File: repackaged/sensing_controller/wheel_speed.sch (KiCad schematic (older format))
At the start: 41 parts, among them J1 CONN_02X03, J2 MM_F_RA_08, U1 MCP2561-E_SN, U101 TPS560430YF, U2 ATMEGA16M1, Y1 Crystal_SMD

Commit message: Change VCC to +5V.
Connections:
- net labels added: +5V
- net labels removed: VCC
- wire segments 109 -> 108
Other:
- note removed: "5V"
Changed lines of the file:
@@
 $Descr A4 11693 8268
 encoding utf-8
-Sheet 1 25
+Sheet 20 25
 Title "Wheel Speed Sensing"
 Date "2019-11-17"
@@
 U 1 1 6102CC1A
 P 6000 6200
-F 0 "R104" V 5800 6200 50  0000 C CNN
-F 1 "R_0_2512" V 5900 6250 50  0000 C CNN
+F 0 "R104" V 5748 6126 50  0000 C CNN
+F 1 "R_0_2512" V 5850 6112 50  0000 C CNN
 F 2 "footprints:R_2512_OEM" H 5930 6200 50  0001 C CNN
 F 3 "http://www.te.com/commerce/DocumentDelivery/DDEController?Action=srchrtrv&DocNm=9-1773463-7&DocType=DS&DocLang=English" H 6080 6200 50  0001 C CNN
@@
 U 1 1 6102CC29
 P 1550 6650
-F 0 "D102" V 1588 6533 50  0000 R CNN
-F 1 "LED_0805" V 1497 6533 50  0000 R CNN
+F 0 "D102" V 1476 6408 50  0000 R CNN
+F 1 "LED_0805" V 1384 6486 50  0000 R CNN
 F 2 "footprints:LED_0805_OEM" H 1450 6650 50  0001 C CNN
 F 3 "http://www.osram-os.com/Graphics/XPic9/00078860_0.pdf" H 1550 6750 50  0001 C CNN
@@
 Text Notes 5800 6100 0    50   ~ 0
 VCC Jumper\n
-$Comp
-L power:VCC #PWR0112
-U 1 1 6102CC26
-P 6400 6050
-F 0 "#PWR0112" H 6400 5900 50  0001 C CNN
-F 1 "VCC" H 6417 6223 50  0000 C CNN
-F 2 "" H 6400 6050 50  0001 C CNN
-F 3 "" H 6400 6050 50  0001 C CNN
-	1    6400 6050
-	1    0    0    -1
-$EndComp
-Text Notes 6500 6000 0    50   ~ 0
-5V
 Text Notes 6250 7300 1    50   ~ 0
 5V Indicator
@@
 U 1 1 6102CC43
 P 4100 4100
-F 0 "Y1" H 3810 4170 50  0000 L CNN
+F 0 "Y1" H 3644 4174 50  0000 L CNN
 F 1 "Crystal_SMD" H 3420 4100 50  0000 L CNN
 F 2 "footprints:Crystal_SMD_FA238" H 4050 4175 50  0001 C CNN
@@
 U 1 1 6102CC46
 P 3900 4350
-F 0 "C4" H 3790 4430 50  0000 L CNN
+F 0 "C4" H 3684 4356 50  0000 L CNN
 F 1 "C_30pF" H 3630 4270 50  0000 L CNN
 F 2 "footprints:C_0805_OEM" H 3938 4200 50  0001 C CNN
@@
 U 1 1 6102CC48
 P 4300 4350
-F 0 "C5" H 4320 4430 50  0000 L CNN
+F 0 "C5" H 4424 4340 50  0000 L CNN
 F 1 "C_30pF" H 4330 4250 50  0000 L CNN
 F 2 "footprints:C_0805_OEM" H 4338 4200 50  0001 C CNN
@@
 $EndComp
 $Comp
-L power:VCC #PWR08
-U 1 1 6102CC54
-P 4450 3350
-F 0 "#PWR08" H 4450 3200 50  0001 C CNN
-F 1 "VCC" H 4560 3410 50  0000 C CNN
-F 2 "" H 4450 3350 50  0001 C CNN
-F 3 "" H 4450 3350 50  0001 C CNN
-	1    4450 3350
-	1    0    0    -1
-$EndComp
-$Comp
 L power:GND #PWR011
 U 1 1 5D5F86E8
@@
 $EndComp
 NoConn ~ 10400 1750
-$Comp
-L power:VCC #PWR01
-U 1 1 5D602F58
-P 9900 1000
-F 0 "#PWR01" H 9900 850 50  0001 C CNN
-F 1 "VCC" H 9917 1173 50  0000 C CNN
-F 2 "" H 9900 1000 50  0001 C CNN
-F 3 "" H 9900 1000 50  0001 C CNN
-	1    9900 1000
-	1    0    0    -1
-$EndComp
 $Comp
 L power:GND #PWR02
@@
 	1    0    0    -1
 $EndComp
-$Comp
-L power:VCC #PWR016
-U 1 1 6102CC6A
-P 10200 6150
-F 0 "#PWR016" H 10200 6000 50  0001 C CNN
-F 1 "VCC" H 10218 6323 50  0000 C CNN
-F 2 "" H 10200 6150 50  0001 C CNN
-F 3 "" H 10200 6150 50  0001 C CNN
-	1    10200 6150
-	-1   0    0    1
-$EndComp
 Text Label 9500 6150 0    50   ~ 0
 5V
-$Comp
-L power:VCC #PWR015
-U 1 1 6102CC6D
-P 9500 6000
-F 0 "#PWR015" H 9500 5850 50  0001 C CNN
-F 1 "VCC" H 9517 6173 50  0000 C CNN
-F 2 "" H 9500 6000 50  0001 C CNN
-F 3 "" H 9500 6000 50  0001 C CNN
-	1    9500 6000
-	1    0    0    -1
-$EndComp
 $Comp
 L power:GND #PWR017
@@
 	1    0    0    -1
 $EndComp
-$Comp
-L power:VCC #PWR07
-U 1 1 5D6297EA
-P 10200 3350
-F 0 "#PWR07" H 10200 3200 50  0001 C CNN
-F 1 "VCC" H 10217 3523 50  0000 C CNN
-F 2 "" H 10200 3350 50  0001 C CNN
-F 3 "" H 10200 3350 50  0001 C CNN
-	1    10200 3350
-	1    0    0    -1
-$EndComp
 Text Notes 8950 3100 0    89   ~ 0
 16M1 PROGRAMMING HEADER\n
-$Comp
-L power:VCC #PWR018
-U 1 1 6102CC79
-P 800 850
-F 0 "#PWR018" H 800 700 50  0001 C CNN
-F 1 "VCC" H 817 1023 50  0000 C CNN
-F 2 "" H 800 850 50  0001 C CNN
-F 3 "" H 800 850 50  0001 C CNN
-	1    800  850
-	1    0    0    -1
-$EndComp
 Wire Wire Line
 	1450 1300 1150 1300
@@
 Connection ~ 1950 6100
 Wire Wire Line
-	1950 6100 2250 6100
-Connection ~ 2250 6100
-Wire Wire Line
-	2250 6100 2500 6100
-Wire Wire Line
 	1550 6400 1550 6500
 Wire Wire Line
@@
 P 5550 1950
 F 0 "J2" H 5700 1450 60  0000 R CNN
-F 1 "MM_F_RA_08" H 5700 2350 60  0000 R CNN
+F 1 "MM_F_RA_08" H 5804 2400 60  0000 R CNN
 F 2 "footprints:micromatch_female_ra_8" H 5450 2250 60  0001 C CNN
 F 3 "http://www.te.com/commerce/DocumentDelivery/DDEController?Action=showdoc&DocId=Customer+Drawing%7F338070%7FG1%7Fpdf%7FEnglish%7FENG_CD_338070_G1.pdf%7F338070-8" H 5550 2350 60  0001 C CNN
@@
 	1    0    0    1
 $EndComp
-Text Notes 5300 900  0    89   ~ 0
+Text Notes 5320 1250 0    89   ~ 0
 CONNECTOR\nPOWER, GND, CAN, SENSOR
 $Comp
@@
 Text Label 5750 4650 2    50   ~ 0
 LEFT_SENSE
-$Comp
-L power:VCC #PWR0115
-U 1 1 5DD30072
-P 6800 3200
-F 0 "#PWR0115" H 6800 3050 50  0001 C CNN
-F 1 "VCC" H 6817 3373 50  0000 C CNN
-F 2 "" H 6800 3200 50  0001 C CNN
-F 3 "" H 6800 3200 50  0001 C CNN
-	1    6800 3200
-	1    0    0    -1
-$EndComp
 Wire Wire Line
 	6800 3300 6800 3200
-$Comp
-L power:VCC #PWR0116
-U 1 1 5DD31D63
-P 6800 4550
-F 0 "#PWR0116" H 6800 4400 50  0001 C CNN
-F 1 "VCC" H 6817 4723 50  0000 C CNN
-F 2 "" H 6800 4550 50  0001 C CNN
-F 3 "" H 6800 4550 50  0001 C CNN
-	1    6800 4550
-	1    0    0    -1
-$EndComp
 Wire Wire Line
 	6800 4550 6800 4650
@@
 	1    0    0    -1
 $EndComp
+Wire Wire Line
+	1950 6100 2500 6100
+$Comp
+L power:+5V #PWR0196
+U 1 1 610910EA
+P 10200 3350
+F 0 "#PWR0196" H 10200 3200 50  0001 C CNN
+F 1 "+5V" H 10215 3523 50  0000 C CNN
+F 2 "" H 10200 3350 50  0001 C CNN
+F 3 "" H 10200 3350 50  0001 C CNN
+	1    10200 3350
+	1    0    0    -1
+$EndComp
+$Comp
+L power:+5V #PWR0192
+U 1 1 61093374
+P 6800 3200
+F 0 "#PWR0192" H 6800 3050 50  0001 C CNN
+F 1 "+5V" H 6815 3373 50  0000 C CNN
+F 2 "" H 6800 3200 50  0001 C CNN
+F 3 "" H 6800 3200 50  0001 C CNN
+	1    6800 3200
+	1    0    0    -1
+$EndComp
+$Comp
+L power:+5V #PWR0193
+U 1 1 61094949
+P 6800 4550
+F 0 "#PWR0193" H 6800 4400 50  0001 C CNN
+F 1 "+5V" H 6815 4723 50  0000 C CNN
+F 2 "" H 6800 4550 50  0001 C CNN
+F 3 "" H 6800 4550 50  0001 C CNN
+	1    6800 4550
+	1    0    0    -1
+$EndComp
+$Comp
+L power:+5V #PWR0194
+U 1 1 61096B13
+P 9500 6000
+F 0 "#PWR0194" H 9500 5850 50  0001 C CNN
+F 1 "+5V" H 9515 6173 50  0000 C CNN
+F 2 "" H 9500 6000 50  0001 C CNN
+F 3 "" H 9500 6000 50  0001 C CNN
+	1    9500 6000
+	1    0    0    -1
+$EndComp
+$Comp
+L power:+5V #PWR?
+U 1 1 6109A447
+P 10200 6150
+AR Path="/60A3D93E/6109A447" Ref="#PWR?"  Part="1"
+AR Path="/60A3DAC4/6109A447" Ref="#PWR0197"  Part="1"
+F 0 "#PWR0197" H 10200 6000 50  0001 C CNN
+F 1 "+5V" H 10215 6323 50  0000 C CNN
+F 2 "" H 10200 6150 50  0001 C CNN
+F 3 "" H 10200 6150 50  0001 C CNN
+	1    10200 6150
+	-1   0    0    1
+$EndComp
+$Comp
+L power:+5V #PWR?
+U 1 1 610A1A4E
+P 6400 6050
+AR Path="/60A3D93E/610A1A4E" Ref="#PWR?"  Part="1"
+AR Path="/60A3DAC4/610A1A4E" Ref="#PWR0191"  Part="1"
+F 0 "#PWR0191" H 6400 5900 50  0001 C CNN
+F 1 "+5V" H 6415 6223 50  0000 C CNN
+F 2 "" H 6400 6050 50  0001 C CNN
+F 3 "" H 6400 6050 50  0001 C CNN
+	1    6400 6050
+	1    0    0    -1
+$EndComp
+$Comp
+L power:+5V #PWR?
+U 1 1 610ADF12
+P 4450 3350
+AR Path="/60A3D93E/610ADF12" Ref="#PWR?"  Part="1"
+AR Path="/60A3DAC4/610ADF12" Ref="#PWR0190"  Part="1"
+F 0 "#PWR0190" H 4450 3200 50  0001 C CNN
+F 1 "+5V" H 4465 3523 50  0000 C CNN
+F 2 "" H 4450 3350 50  0001 C CNN
+F 3 "" H 4450 3350 50  0001 C CNN
+	1    4450 3350
+	1    0    0    -1
+$EndComp
+$Comp
+L power:+5V #PWR?
+U 1 1 610B6FAB
+P 800 850
+AR Path="/60A3D93E/610B6FAB" Ref="#PWR?"  Part="1"
+AR Path="/60A3DAC4/610B6FAB" Ref="#PWR0189"  Part="1"
+F 0 "#PWR0189" H 800 700 50  0001 C CNN
+F 1 "+5V" H 815 1023 50  0000 C CNN
+F 2 "" H 800 850 50  0001 C CNN
+F 3 "" H 800 850 50  0001 C CNN
+	1    800  850
+	1    0    0    -1
+$EndComp
+$Comp
+L power:+5V #PWR?
+U 1 1 610BDB5E
+P 9900 1000
+AR Path="/60A3D93E/610BDB5E" Ref="#PWR?"  Part="1"
+AR Path="/60A3DAC4/610BDB5E" Ref="#PWR0195"  Part="1"
+F 0 "#PWR0195" H 9900 850 50  0001 C CNN
+F 1 "+5V" H 9915 1173 50  0000 C CNN
+F 2 "" H 9900 1000 50  0001 C CNN
+F 3 "" H 9900 1000 50  0001 C CNN
+	1    9900 1000
+	1    0    0    -1
+$EndComp

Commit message: Fixed net labels and add missing components.
Changed power flags to global net labels, connected strain gauge nets to ATMEGA16M1, added LEDs where needed, and changed net labels to connect as needed.
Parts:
- removed C6: C_0.1uF, footprints:C_0805_OEM, symbol formula:C_0.1uF
- removed D2, D3: LED_0805, footprints:LED_0805_OEM, symbol formula:LED_0805
- removed J2: MM_F_RA_08, footprints:micromatch_female_ra_8, symbol formula:MM_F_RA_08
- removed JP1: FRONT_BACK, Jumper:SolderJumper-2_P1.3mm_Open_RoundedPad1.0x1.5mm, symbol Device:Jumper_NO_Small
- removed JP2: LEFT_RIGHT, Jumper:SolderJumper-2_P1.3mm_Open_RoundedPad1.0x1.5mm, symbol Device:Jumper_NO_Small
- removed R4, R5: R_10K, footprints:R_0805_OEM, symbol formula:R_10K
- removed R6, R7: R_200, footprints:R_0805_OEM, symbol formula:R_200
- added D12, D13: LED_0805, footprints:LED_0805_OEM, symbol formula:LED_0805
- added R119, R120: R_10K, footprints:R_0805_OEM, symbol formula:R_10K
- added R121, R122: R_0, footprints:R_0603_1608Metric, symbol formula:R_0
- added R124, R125: R_200, footprints:R_0805_OEM, symbol formula:R_200
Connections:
- wire segments 108 -> 100
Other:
- note removed: "CONNECTOR\nPOWER, GND, CAN, SENSOR"

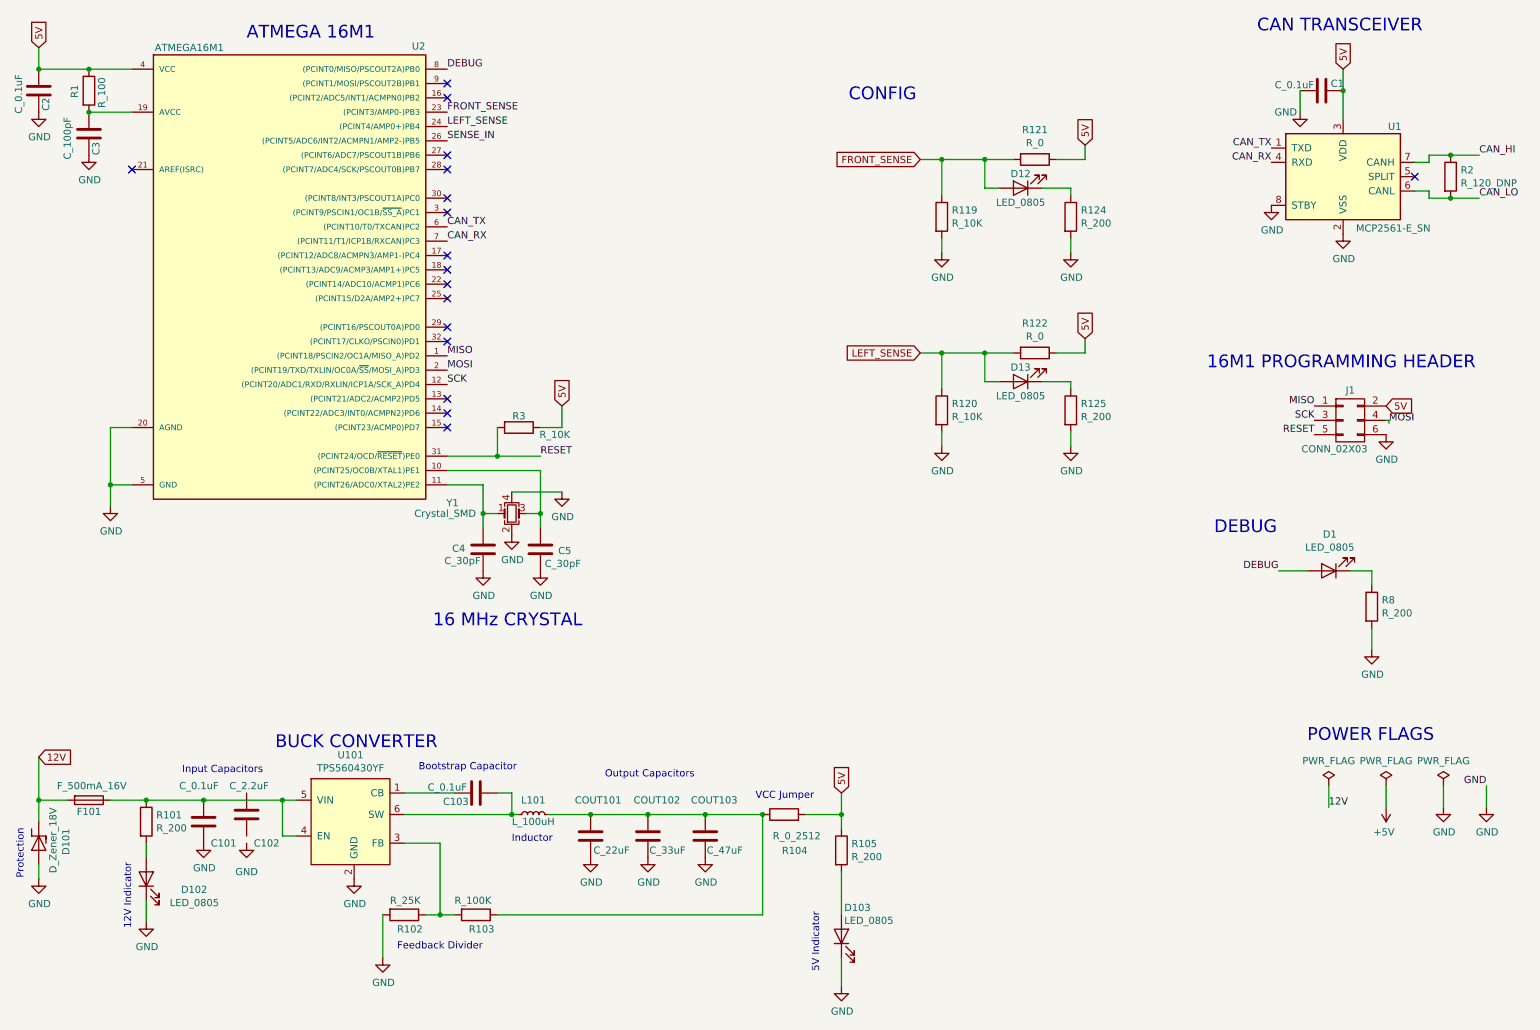
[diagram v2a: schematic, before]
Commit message: Add space between net labels and block.
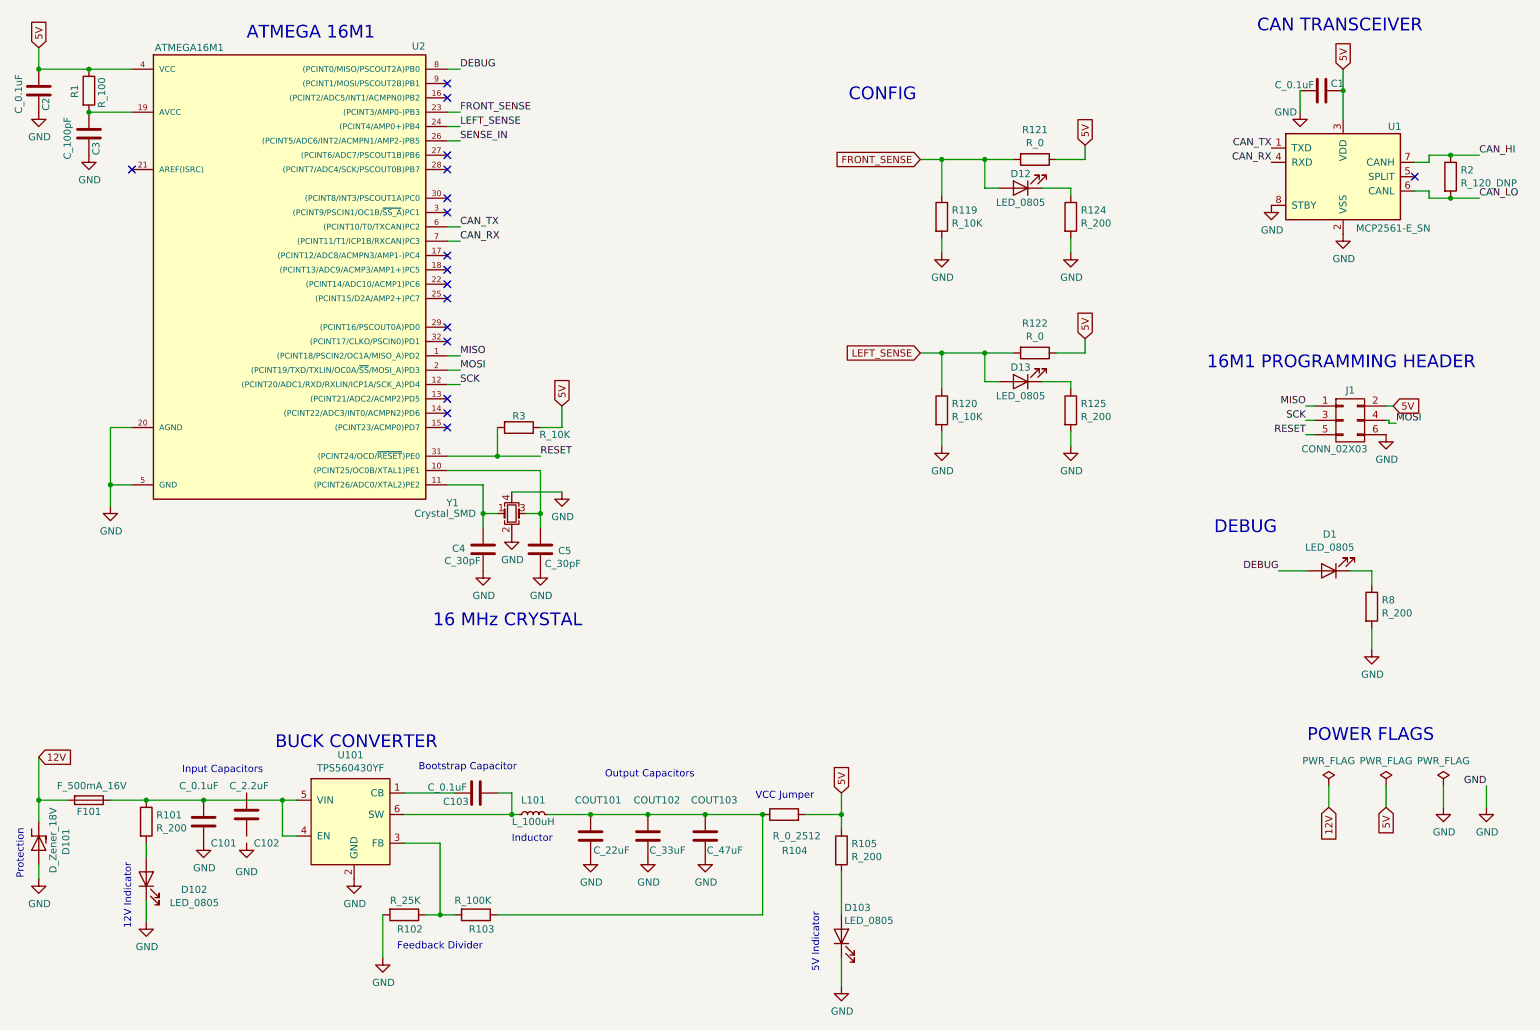
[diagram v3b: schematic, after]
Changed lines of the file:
@@
 $Comp
 L power:GND #PWR0106
-U 1 1 5BEE119A
+U 1 1 613BE4F9
 P 3000 6650
 F 0 "#PWR0106" H 3000 6400 50  0001 C CNN
@@
 $Comp
 L power:GND #PWR0105
-U 1 1 5BEE168D
+U 1 1 613BE4FB
 P 2250 6400
 F 0 "#PWR0105" H 2250 6150 50  0001 C CNN
@@
 	1    0    0    -1
 $EndComp
-Text Label 9800 6150 0    50   ~ 0
-12V
 $Comp
 L formula:C_22uF COUT101
@@
 $Comp
 L formula:R_25K R102
-U 1 1 5C0B315C
+U 1 1 613BE508
 P 3350 6900
 F 0 "R102" V 3450 6850 50  0000 L CNN
@@
 	1    0    0    -1
 $EndComp
-Text Label 3650 2100 0    50   ~ 0
+Text Label 3740 2100 0    50   ~ 0
 CAN_TX
-Text Label 3650 2200 0    50   ~ 0
+Text Label 3740 2200 0    50   ~ 0
 CAN_RX
-Text Label 3650 3000 0    50   ~ 0
+Text Label 3740 3000 0    50   ~ 0
 MISO
-Text Label 3650 3100 0    50   ~ 0
+Text Label 3740 3100 0    50   ~ 0
 MOSI
-Text Label 3650 3200 0    50   ~ 0
+Text Label 3740 3200 0    50   ~ 0
 SCK
 Text Label 4300 3700 0    50   ~ 0
@@
 $Comp
 L power:GND #PWR017
-U 1 1 5D622997
+U 1 1 613BE536
 P 10900 6150
 F 0 "#PWR017" H 10900 5900 50  0001 C CNN
@@
 Text Label 10900 6000 2    50   ~ 0
 GND
-Text Label 9700 3350 2    50   ~ 0
+Text Label 9640 3350 2    50   ~ 0
 MISO
-Text Label 9700 3450 2    50   ~ 0
+Text Label 9640 3450 2    50   ~ 0
 SCK
-Text Label 9700 3550 2    50   ~ 0
+Text Label 9640 3550 2    50   ~ 0
 RESET
-Text Label 10220 3470 0    50   ~ 0
+Text Label 10270 3470 0    50   ~ 0
 MOSI
 $Comp
@@
 Wire Wire Line
 	10400 1850 10500 1850
-Text Label 3650 1500 0    50   ~ 0
+Text Label 3740 1500 0    50   ~ 0
 SENSE_IN
-Text Label 3650 1300 0    50   ~ 0
+Text Label 3740 1300 0    50   ~ 0
 FRONT_SENSE
-Text Label 3650 1400 0    50   ~ 0
+Text Label 3740 1400 0    50   ~ 0
 LEFT_SENSE
 NoConn ~ 3650 1100
@@
 Text Notes 9000 4250 0    89   ~ 0
 DEBUG
-Text Label 3650 1000 0    50   ~ 0
+Text Label 3740 1000 0    50   ~ 0
 DEBUG
 Text Label 9450 4500 2    50   ~ 0
@@
 Wire Wire Line
 	1950 6100 2500 6100
-$Comp
-L power:+5V #PWR?
-U 1 1 6109A447
-P 10200 6150
-AR Path="/60A3D93E/6109A447" Ref="#PWR?"  Part="1"
-AR Path="/60A3DAC4/6109A447" Ref="#PWR0197"  Part="1"
-F 0 "#PWR0197" H 10200 6000 50  0001 C CNN
-F 1 "+5V" H 10215 6323 50  0000 C CNN
-F 2 "" H 10200 6150 50  0001 C CNN
-F 3 "" H 10200 6150 50  0001 C CNN
-	1    10200 6150
-	-1   0    0    1
-$EndComp
 Text GLabel 800  850  1    50   Input ~ 0
 5V
@@
 	1    0    0    -1
 $EndComp
-Text GLabel 10200 3350 2    50   Input ~ 0
+Text GLabel 10250 3350 2    50   Input ~ 0
 5V
 Wire Wire Line
@@
 $EndComp
 Connection ~ 7400 2980
+Text GLabel 10200 6150 3    50   Input ~ 0
+5V
+Text GLabel 9800 6150 3    50   Input ~ 0
+12V
+Wire Wire Line
+	9640 3350 9700 3350
+Wire Wire Line
+	9640 3450 9700 3450
+Wire Wire Line
+	9640 3550 9700 3550
+Wire Wire Line
+	10200 3350 10250 3350
+Wire Wire Line
+	10220 3470 10270 3470
+Wire Wire Line
+	3650 1000 3740 1000
+Wire Wire Line
+	3650 1300 3740 1300
+Wire Wire Line
+	3650 1400 3740 1400
+Wire Wire Line
+	3650 1500 3740 1500
+Wire Wire Line
+	3650 2100 3740 2100
+Wire Wire Line
+	3740 2200 3650 2200
+Wire Wire Line
+	3650 3000 3740 3000
+Wire Wire Line
+	3650 3100 3740 3100
+Wire Wire Line
+	3650 3200 3740 3200
 $EndSCHEMATC
